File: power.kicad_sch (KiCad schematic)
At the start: 22 parts, among them Q21 AO3400A, Q22 AO3400A, Q23 AO3400A, U11 ADP2302ARDZ-5.0, U13 XC6206PxxxMR - C5446

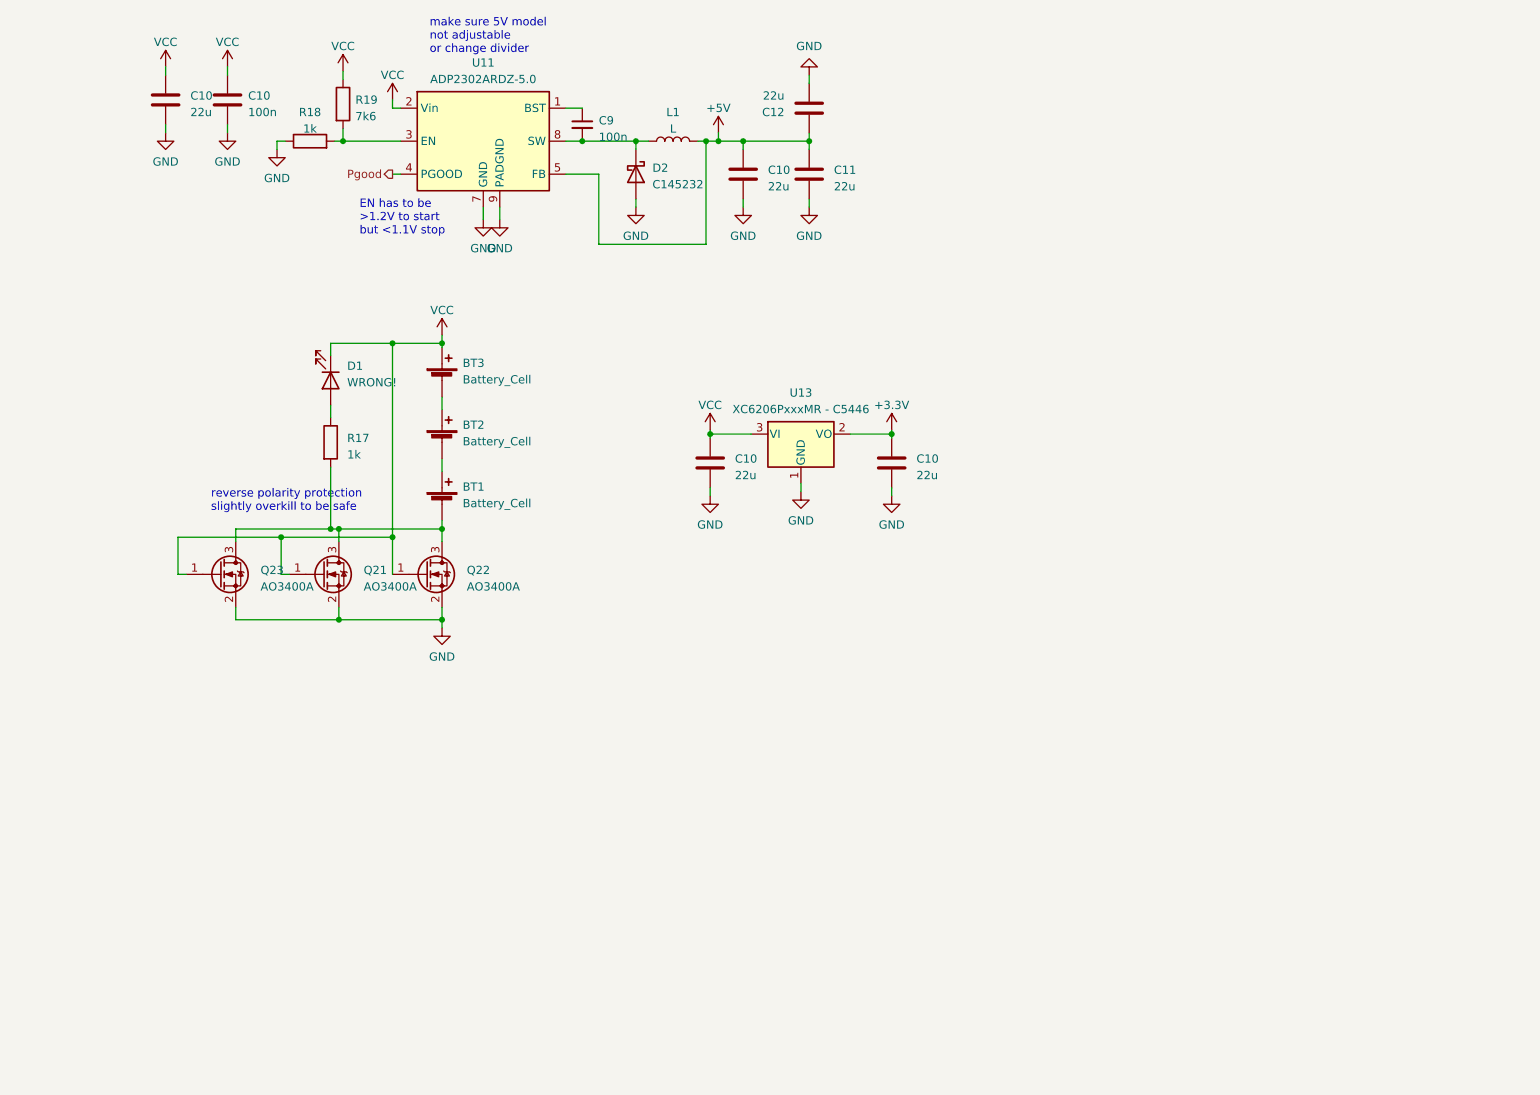
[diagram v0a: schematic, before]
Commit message: routing of H bridges and servo power pins
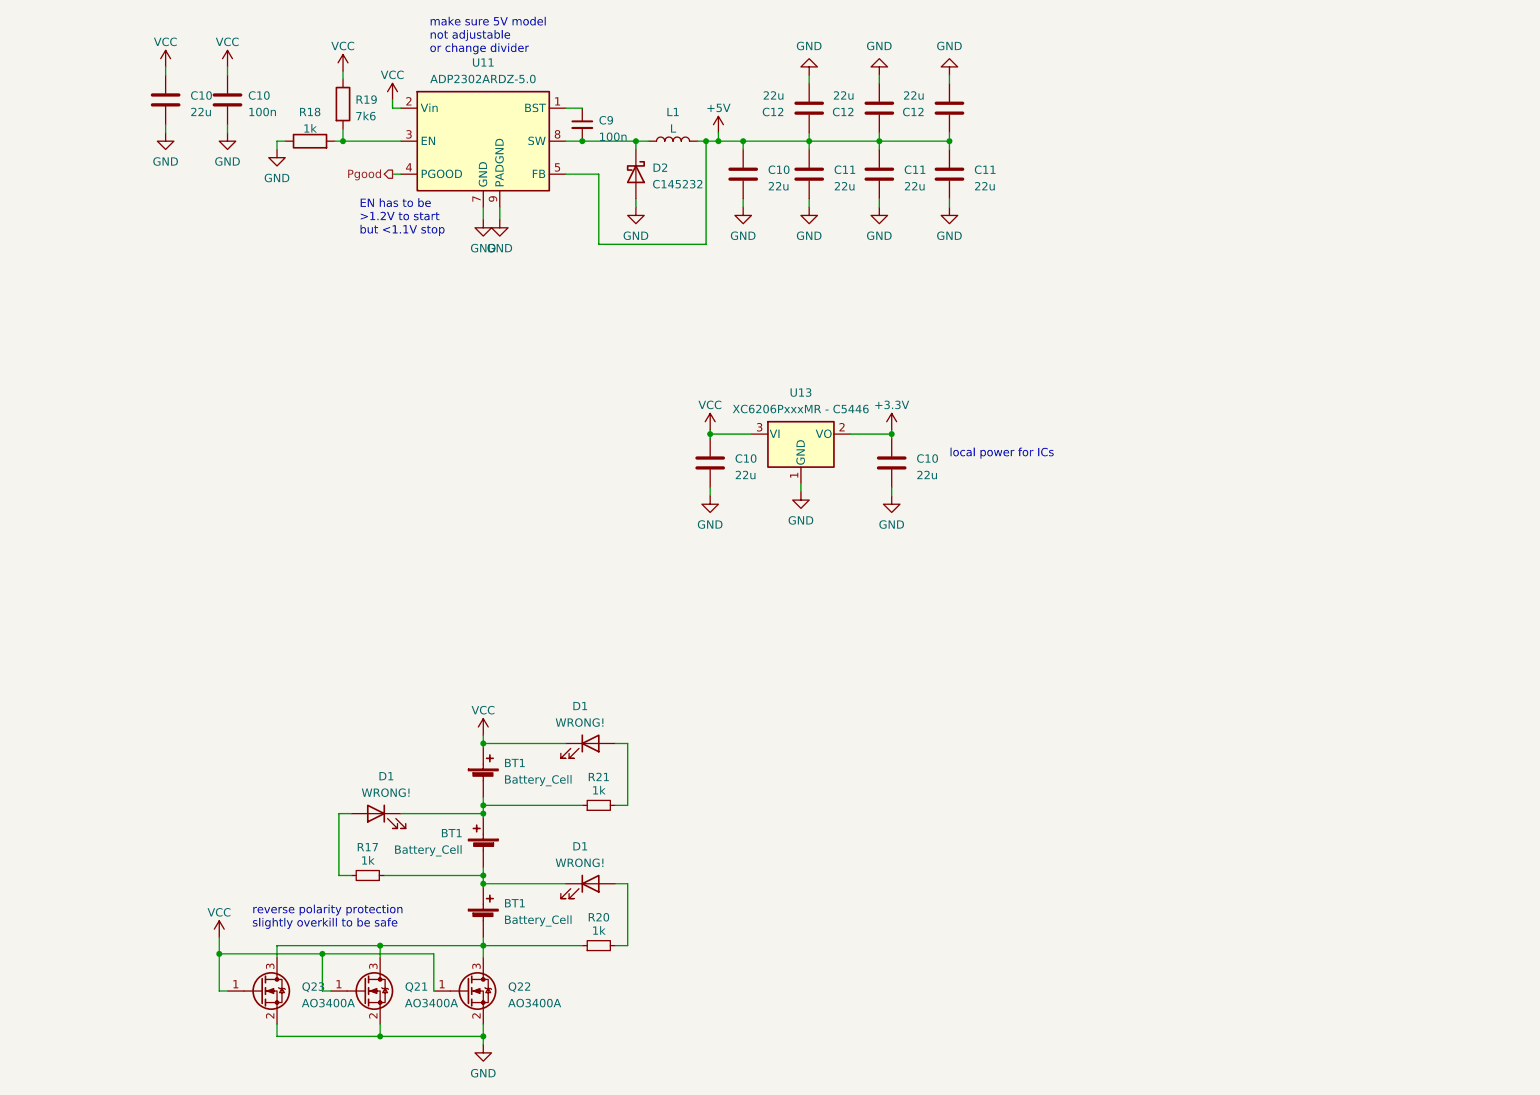
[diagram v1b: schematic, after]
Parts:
- removed BT2, BT3: Battery_Cell, symbol Device:Battery_Cell
- removed R17: 1k, symbol Device:R
- added BT1 (x2): Battery_Cell, symbol Device:Battery_Cell
- added C11 (x2), C12 (x2): 22u, Capacitor_SMD:C_0805_2012Metric_Pad1.18x1.45mm_HandSolder, symbol Device:C
- added D1 (x2): WRONG!, Diode_SMD:D_0805_2012Metric_Pad1.15x1.40mm_HandSolder, symbol Device:LED
- added R17, R20, R21: 1k, Resistor_SMD:R_0603_1608Metric_Pad0.98x0.95mm_HandSolder, symbol Device:R_Small
- C10, C11, C12: footprint (none) -> Capacitor_SMD:C_0805_2012Metric_Pad1.18x1.45mm_HandSolder
- C10, C9: footprint (none) -> Capacitor_SMD:C_0603_1608Metric_Pad1.08x0.95mm_HandSolder
- D1: footprint (none) -> Diode_SMD:D_0805_2012Metric_Pad1.15x1.40mm_HandSolder
- D2: footprint (none) -> Diode_SMD:D_SMA_Handsoldering
- R18, R19: footprint (none) -> Resistor_SMD:R_0603_1608Metric_Pad0.98x0.95mm_HandSolder
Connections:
- net +5V: now also C11.1, C11.1, C12.1, C12.1
- net GND: now also C11.2, C11.2, C12.2, C12.2
- net VCC: now also BT1.1 (+), D1.1 (K); no longer D1.1 (K)
- net at D1.2 (A): now also R20.2
- net at BT1.2 (-), Q21.3 (D), Q22.3 (D)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: now also R20.1
- net at BT1.1 (+): now also D1.1 (K), BT1.2 (-), R17.1
- new net: D1.2 (A), R21.2
- new net: BT1.1 (+), BT1.2 (-), D1.1 (K), R21.1
- new net: D1.2 (A), R17.2
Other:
- note added: "local power for ICs"
- moved on the sheet: BT1, D1, Q21, Q22, Q23

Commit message: footprint for 18650 holder example pcb battery layout
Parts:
- BT1: footprint (none) -> 18650:single
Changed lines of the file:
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@@
       (effects (font (size 1.27 1.27)) (justify left))
     )
-    (property "Footprint" "" (at 67.945 141.986 90)
+    (property "Footprint" "18650:single" (at 67.945 141.986 90)
       (effects (font (size 1.27 1.27)) hide)
     )
@@
       (effects (font (size 1.27 1.27)) (justify left))
     )
-    (property "Footprint" "" (at 67.945 131.191 90)
+    (property "Footprint" "18650:single" (at 67.945 131.191 90)
       (effects (font (size 1.27 1.27)) hide)
     )
@@
       (effects (font (size 1.27 1.27)) (justify left))
     )
-    (property "Footprint" "" (at 67.945 152.781 90)
-      (effects (font (size 1.27 1.27)) hide)
-    )
+    (property "Footprint" "18650:single" (at 67.945 152.781 90)
+      (effects (font (size 1.27 1.27)) hide)
+    )

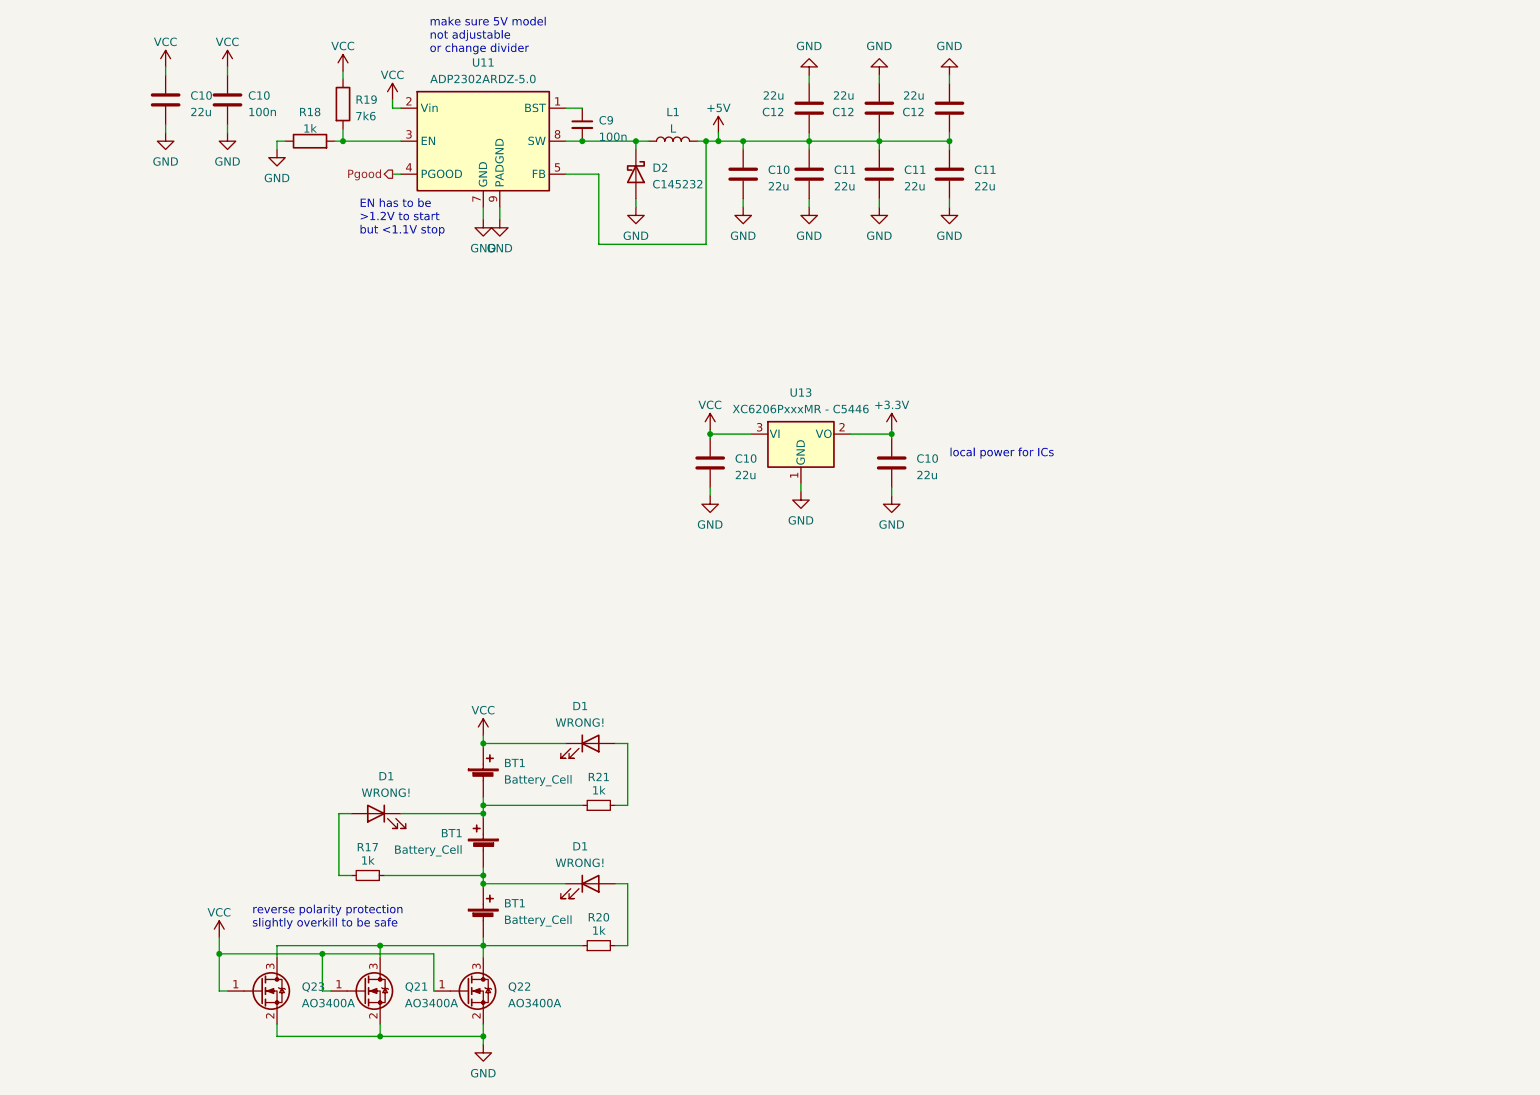
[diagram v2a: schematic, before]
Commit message: more capacitance near motors 16x22uF total 3S->2S
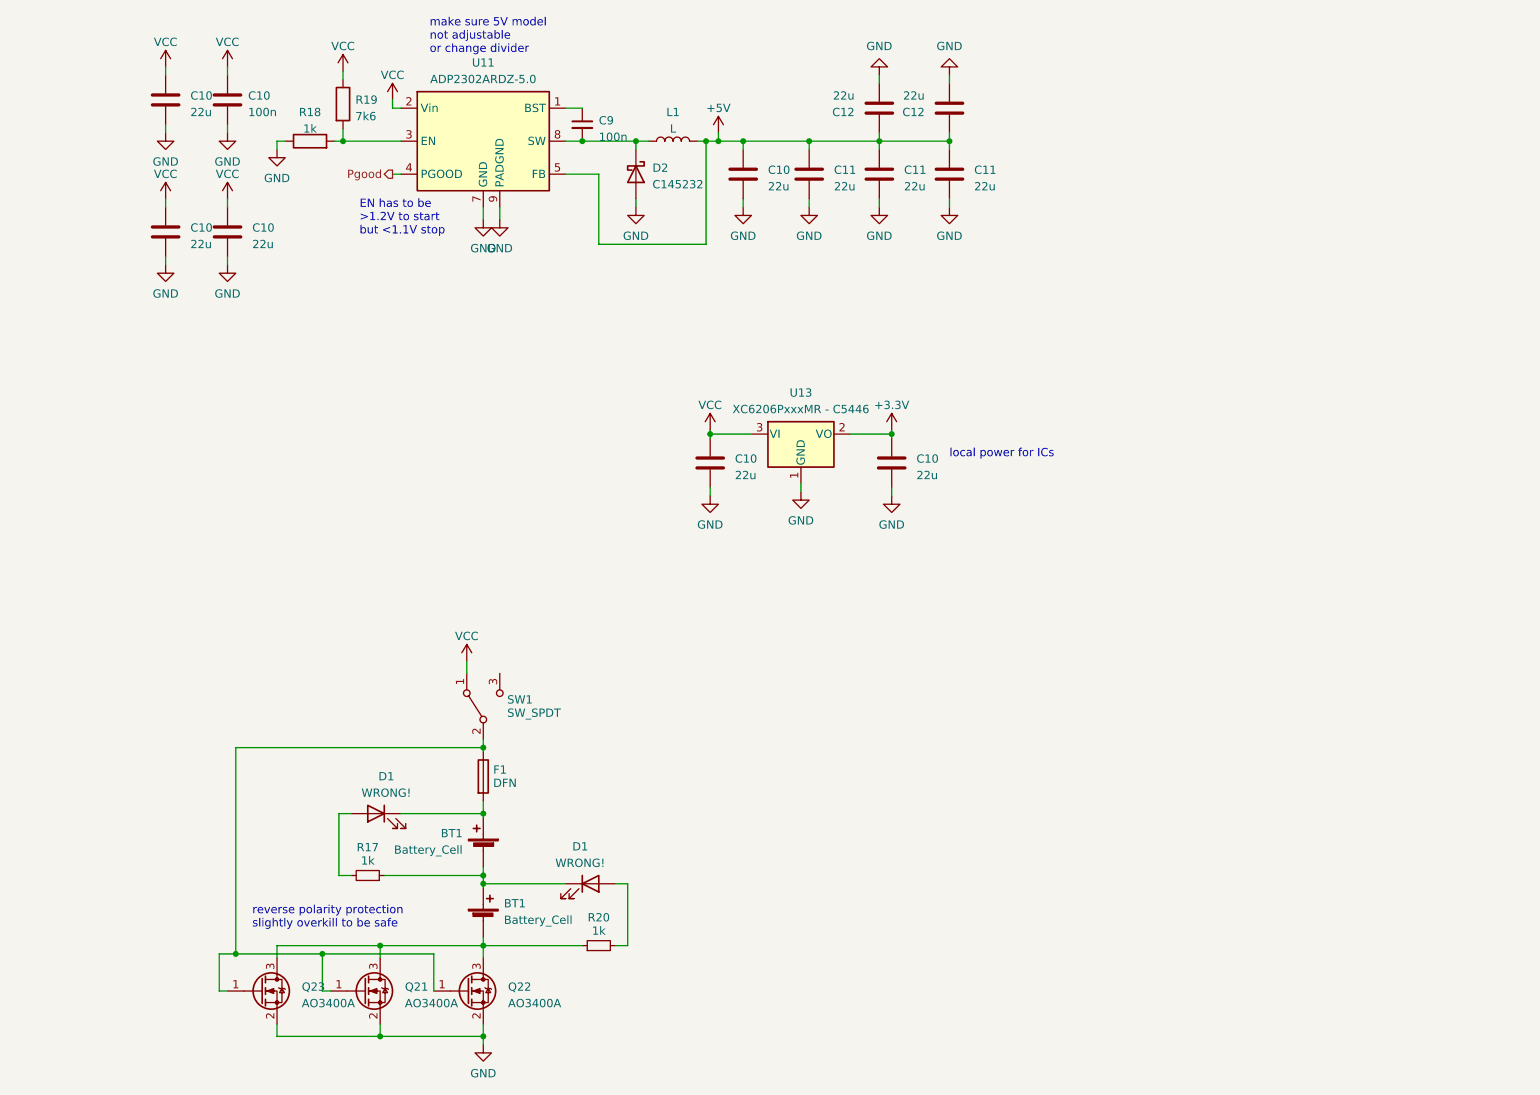
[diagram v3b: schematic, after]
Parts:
- removed BT1: Battery_Cell, 18650:single, symbol Device:Battery_Cell
- removed C12: 22u, Capacitor_SMD:C_0805_2012Metric_Pad1.18x1.45mm_HandSolder, symbol Device:C
- removed D1: WRONG!, Diode_SMD:D_0805_2012Metric_Pad1.15x1.40mm_HandSolder, symbol Device:LED
- removed R21: 1k, Resistor_SMD:R_0603_1608Metric_Pad0.98x0.95mm_HandSolder, symbol Device:R_Small
- added C10 (x2): 22u, Capacitor_SMD:C_0805_2012Metric_Pad1.18x1.45mm_HandSolder, symbol Device:C
- added F1: DFN, Fuse:Fuse_1210_3225Metric_Pad1.42x2.65mm_HandSolder, symbol Device:Fuse
- added SW1: SW_SPDT, symbol Switch:SW_SPDT
- L1: footprint (none) -> Inductor_SMD:L_Changjiang_FNR5020S
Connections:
- net GND: now also C10.2, C10.2
- net VCC: now also C10.1, C10.1, SW1.1 (A); no longer Q21.1 (G), Q22.1 (G), Q23.1 (G)
- net at BT1.1 (+), D1.1 (K): now also F1.2
- new net: F1.1, Q21.1 (G), Q22.1 (G), Q23.1 (G), SW1.2 (B)

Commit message: verison 1.0 just routed
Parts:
- removed C10 (x2): 22u, Capacitor_SMD:C_0805_2012Metric_Pad1.18x1.45mm_HandSolder, symbol Device:C
- removed U13: XC6206PxxxMR - C5446, Package_TO_SOT_SMD:SOT-23-3, symbol Regulator_Linear:XC6206PxxxMR
- added D1: PWR, Diode_SMD:D_0805_2012Metric_Pad1.15x1.40mm_HandSolder, symbol Device:LED
- added Q21, Q23: AO3400A, Package_TO_SOT_SMD:SOT-23, symbol Transistor_FET:AO3400A
- added R24: 4k, Resistor_SMD:R_0603_1608Metric_Pad0.98x0.95mm_HandSolder, symbol Device:R_Small
- R19: value 7k6 -> 4k
- SW1: footprint (none) -> switches:TSM1x3
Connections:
- net GND: now also Q21.2 (S), Q23.2 (S), R24.1
- net VCC: now also SW1.2 (B), D1.2 (A)
- net at Q21.1 (G), Q22.1 (G), Q23.1 (G): now also BT1.1 (+), D1.1 (K), F1.2, Q21.1 (G), Q23.1 (G); no longer F1.1, SW1.2 (B)
- net at BT1.2 (-), Q21.3 (D), Q22.3 (D)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: now also Q21.3 (D), Q23.3 (D)
- net at SW1.3 (C): now also F1.1
- new net: D1.1 (K), R24.2
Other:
- note added: "batteries can go as low as 6V total"
- note added: "for ease of routing"
- note removed: "local power for ICs"
- moved on the sheet: SW1

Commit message: new version of layout with diodes improved power routing a little bit
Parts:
- L1: footprint Inductor_SMD:L_Changjiang_FNR5020S -> Inductor_SMD:L_Changjiang_FNR6045S
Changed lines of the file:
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@@
       (effects (font (size 1.27 1.27)))
     )
-    (property "Footprint" "Inductor_SMD:L_Changjiang_FNR5020S" (at 97.155 34.29 0)
+    (property "Footprint" "Inductor_SMD:L_Changjiang_FNR6045S" (at 97.155 34.29 0)
       (effects (font (size 1.27 1.27)) hide)
     )

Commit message: added moany componaets
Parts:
- removed BT1 (x2): Battery_Cell, 18650:single, symbol Device:Battery_Cell
- removed D1 (x2): WRONG!, Diode_SMD:D_0805_2012Metric_Pad1.15x1.40mm_HandSolder, symbol Device:LED
- added D? (x3): WRONG!, Diode_SMD:D_0805_2012Metric_Pad1.15x1.40mm_HandSolder, symbol Device:LED
- added R27: 1k, Resistor_SMD:R_0603_1608Metric_Pad0.98x0.95mm_HandSolder, symbol Device:R_Small
- added U14: BH-18650-B5BA016, footprint:BAT-SMD_BH-18650-B5BA016, symbol BH-18650-B5BA016:BH-18650-B5BA016
- D?: renamed from D2; JLCPCB Part# (none) -> C145232
- Q?: renamed from Q21; JLCPCB Part# (none) -> C20917
- renumbered C10 to C?, C12 to C?, C11 to C?, C9 to C?, D1 to D?, L1 to L?, Q23 to Q?, Q22 to Q?, Q21 to Q?, R19 to R?, R18 to R?, U11 to U?
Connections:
- net VCC: now also Q?.1 (G), Q?.1 (G), Q?.1 (G), Q?.1 (G), Q?.1 (G)
- net at Q?.3 (D), Q?.3 (D), Q?.3 (D)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: now also D?.2 (A), U14.6; no longer R20.1
- net at R17.1: now also D?.1 (K)
- net at R20.2: now also D?.2 (A), U14.4, U14.5
- net at R17.2: now also D?.2 (A), U14.2, U14.3
- new net: D?.1 (K), R20.1
- new net: D?.1 (K), R27.1
- new net: F1.2, R27.2, U14.1
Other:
- note added: "+"
- note added: "-"
- moved on the sheet: D?, Q?, R24, SW1
